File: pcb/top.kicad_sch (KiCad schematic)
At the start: 77 parts, among them J1 Conn_01x01, J10 Conn_01x01, J11 Conn_01x01, J2 Conn_01x01, J3 Conn_01x06, J4 Conn_01x01, J5 Conn_01x01, J6 Conn_01x01, J7 Conn_01x01, J8 Conn_01x01, J9 Conn_01x01, Q1 2N7002, Q2 2N7002, Q3 2N7002, Q4 2N7002, U1 L78L05_SOT89, U2 PIC12F629-ISN, U3 L78L08_SO8

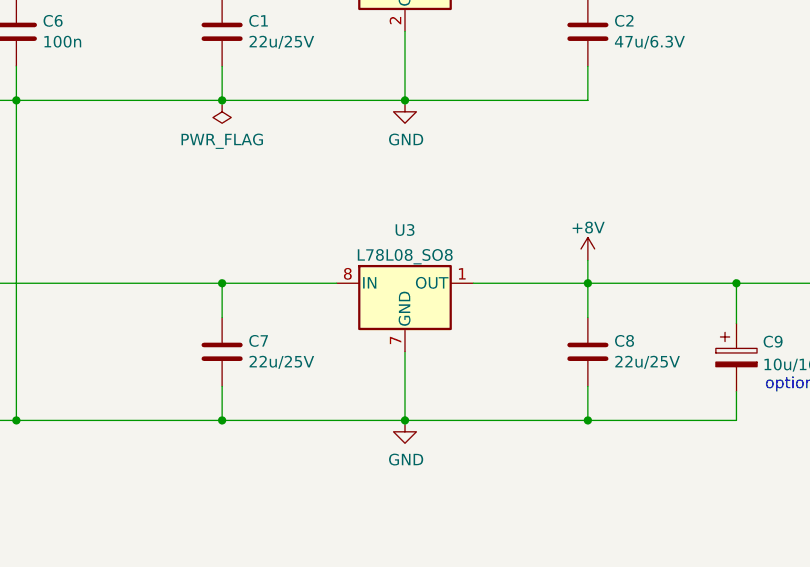
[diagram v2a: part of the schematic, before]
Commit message: Use SOT89 for 78L08.
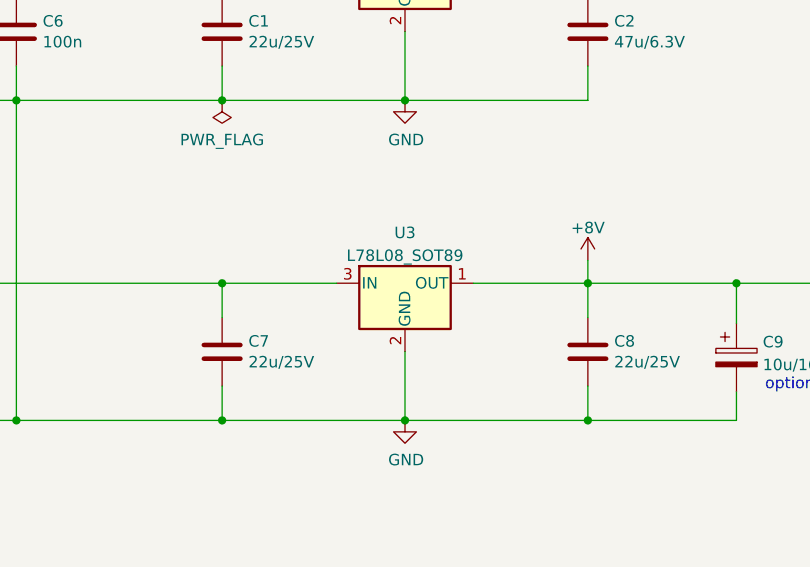
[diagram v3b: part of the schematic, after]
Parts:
- removed U3: L78L08_SO8, Package_SO:SOIC-8_3.9x4.9mm_P1.27mm, symbol Regulator_Linear:L78L08_SO8
- added U3: L78L08_SOT89, Package_TO_SOT_SMD:SOT-89-3_Handsoldering, symbol Regulator_Linear:L78L08_SOT89
- R1, R21: JLCPCB_IGNORE true -> (none); LCSC (none) -> C364154
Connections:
- net +15V: now also U3.3 (IN)
- net +8V: now also U3.1 (OUT)
- net GND: now also U3.2 (GND)
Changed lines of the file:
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@@
       (effects (font (size 1.27 1.27)) hide)
     )
-    (property "LCSC" "" (id 4) (at 67.31 81.28 0)
-      (effects (font (size 1.27 1.27)) hide)
-    )
-    (property "JLCPCB_IGNORE" "true" (id 5) (at 67.31 81.28 0)
+    (property "LCSC" "C364154" (id 4) (at 67.31 81.28 0)
+      (effects (font (size 1.27 1.27)) hide)
+    )
+    (property "JLCPCB_IGNORE" "" (id 5) (at 67.31 81.28 0)
       (effects (font (size 1.27 1.27)) hide)
     )
@@
     )
   )
-  (symbol (lib_id "Regulator_Linear:L78L08_SO8") (at 135.89 72.39 0) (unit 1)
+  (symbol (lib_id "Mechanical:MountingHole") (at 76.2 176.53 0) (unit 1)
+    (in_bom yes) (on_board yes)
+    (property "Reference" "H9" (id 0) (at 78.74 175.3616 0)
+      (effects (font (size 1.27 1.27)) (justify left))
+    )
+    (property "Value" "MountingHole" (id 1) (at 78.74 177.673 0)
+      (effects (font (size 1.27 1.27)) (justify left))
+    )
+    (property "Footprint" "MountingHole:MountingHole_2.2mm_M2" (id 2) (at 76.2 176.53 0)
+      (effects (font (size 1.27 1.27)) hide)
+    )
+    (property "Datasheet" "~" (id 3) (at 76.2 176.53 0)
+      (effects (font (size 1.27 1.27)) hide)
+    )
+    (property "JLCPCB_IGNORE" "true" (id 4) (at 76.2 176.53 0)
+      (effects (font (size 1.27 1.27)) hide)
+    )
+  )
+  (symbol (lib_id "Regulator_Linear:L78L08_SOT89") (at 135.89 72.39 0) (unit 1)
     (in_bom yes) (on_board yes) (fields_autoplaced)
-    (property "Reference" "U3" (id 0) (at 135.89 66.5185 0))
-    (property "Value" "L78L08_SO8" (id 1) (at 135.89 69.2936 0))
-    (property "Footprint" "Package_SO:SOIC-8_3.9x4.9mm_P1.27mm" (id 2) (at 138.43 67.31 0)
+    (property "Reference" "U3" (id 0) (at 135.89 66.7852 0))
+    (property "Value" "L78L08_SOT89" (id 1) (at 135.89 69.3221 0))
+    (property "Footprint" "Package_TO_SOT_SMD:SOT-89-3_Handsoldering" (id 2) (at 135.89 67.31 0)
       (effects (font (size 1.27 1.27) italic) hide)
     )
-    (property "Datasheet" "http://www.st.com/content/ccc/resource/technical/document/datasheet/15/55/e5/aa/23/5b/43/fd/CD00000446.pdf/files/CD00000446.pdf/jcr:content/translations/en.CD00000446.pdf" (id 3) (at 140.97 72.39 0)
+    (property "Datasheet" "http://www.st.com/content/ccc/resource/technical/document/datasheet/15/55/e5/aa/23/5b/43/fd/CD00000446.pdf/files/CD00000446.pdf/jcr:content/translations/en.CD00000446.pdf" (id 3) (at 135.89 73.66 0)
+      (effects (font (size 1.27 1.27)) hide)
+    )
+    (property "LCSC" "C122846" (id 4) (at 135.89 72.39 0)
       (effects (font (size 1.27 1.27)) hide)
     )
@@
     (pin "2")
     (pin "3")
-    (pin "4")
-    (pin "5")
-    (pin "6")
-    (pin "7")
-    (pin "8")
-  )
-  (symbol (lib_id "Mechanical:MountingHole") (at 76.2 176.53 0) (unit 1)
-    (in_bom yes) (on_board yes)
-    (property "Reference" "H9" (id 0) (at 78.74 175.3616 0)
-      (effects (font (size 1.27 1.27)) (justify left))
-    )
-    (property "Value" "MountingHole" (id 1) (at 78.74 177.673 0)
-      (effects (font (size 1.27 1.27)) (justify left))
-    )
-    (property "Footprint" "MountingHole:MountingHole_2.2mm_M2" (id 2) (at 76.2 176.53 0)
-      (effects (font (size 1.27 1.27)) hide)
-    )
-    (property "Datasheet" "~" (id 3) (at 76.2 176.53 0)
-      (effects (font (size 1.27 1.27)) hide)
-    )
-    (property "JLCPCB_IGNORE" "true" (id 4) (at 76.2 176.53 0)
-      (effects (font (size 1.27 1.27)) hide)
-    )
   )
   (symbol (lib_id "Device:R") (at 261.62 116.84 0) (mirror y) (unit 1)
@@
       (effects (font (size 1.27 1.27)) hide)
     )
-    (property "LCSC" "" (id 4) (at 261.62 116.84 0)
-      (effects (font (size 1.27 1.27)) hide)
-    )
-    (property "JLCPCB_IGNORE" "true" (id 5) (at 261.62 116.84 0)
+    (property "LCSC" "C364154" (id 4) (at 261.62 116.84 0)
+      (effects (font (size 1.27 1.27)) hide)
+    )
+    (property "JLCPCB_IGNORE" "" (id 5) (at 261.62 116.84 0)
       (effects (font (size 1.27 1.27)) hide)
     )
@@
       (reference "U2") (unit 1) (value "PIC12F629-ISN") (footprint "Package_SO:SOIC-8_3.9x4.9mm_P1.27mm")
     )
-    (path "/3b696e07-76f1-4f5e-aafe-cd6072c0e837"
-      (reference "U3") (unit 1) (value "L78L08_SO8") (footprint "Package_SO:SOIC-8_3.9x4.9mm_P1.27mm")
-    )
-  )
+    (path "/51343116-0c24-4c32-9cad-797ee49a352e"
+      (reference "U3") (unit 1) (value "L78L08_SOT89") (footprint "Package_TO_SOT_SMD:SOT-89-3_Handsoldering")
+    )
+  )

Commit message: Correct JLCPCB parts orientation.
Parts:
- U2: JLCPCB_CORRECTION (none) -> 0;0;-90
- U3: JLCPCB_CORRECTION (none) -> 0;0;180
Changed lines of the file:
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@@
+      (effects (font (size 1.27 1.27)) hide)
+    )
+    (property "JLCPCB_CORRECTION" "0;0;-90" (id 5) (at 152.4 135.89 0)
       (effects (font (size 1.27 1.27)) hide)
     )
@@
       (effects (font (size 1.27 1.27)) hide)
     )
+    (property "JLCPCB_CORRECTION" "0;0;180" (id 5) (at 135.89 72.39 0)
+      (effects (font (size 1.27 1.27)) hide)
+    )

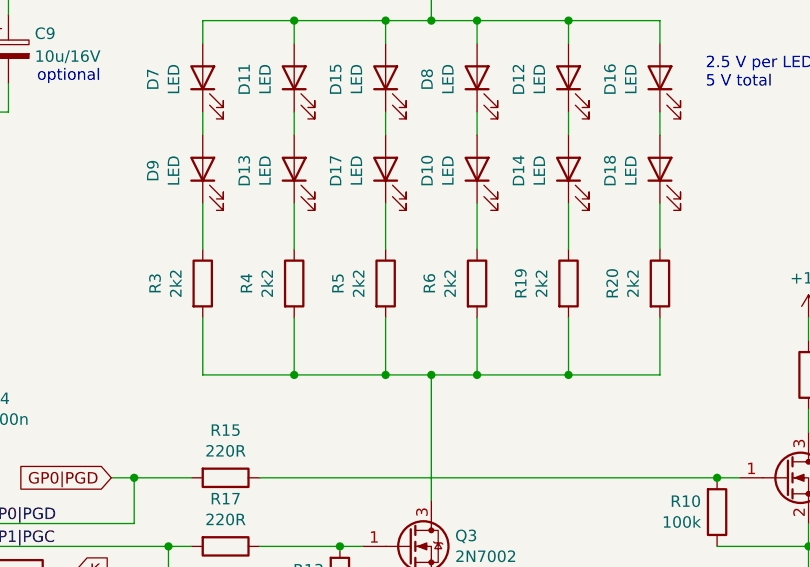
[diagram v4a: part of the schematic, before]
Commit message: Enalarge interior LEDs resistors to 4k7.
Light wa too bright.
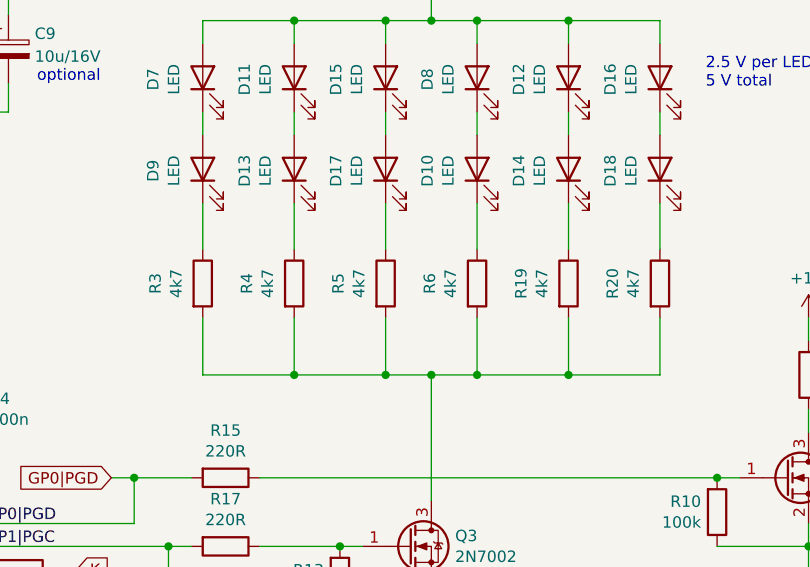
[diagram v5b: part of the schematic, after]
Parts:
- R19, R20, R3, R4, R5, R6: value 2k2 -> 4k7; LCSC C17520 -> C17673
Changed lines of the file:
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@@
     (in_bom yes) (on_board yes)
     (property "Reference" "R4" (id 0) (at 199.2122 106.68 90))
-    (property "Value" "2k2" (id 1) (at 201.5236 106.68 90))
+    (property "Value" "4k7" (id 1) (at 201.5236 106.68 90))
     (property "Footprint" "Resistor_SMD:R_0805_2012Metric_Pad1.20x1.40mm_HandSolder" (id 2) (at 202.692 106.68 90)
       (effects (font (size 1.27 1.27)) hide)
@@
       (effects (font (size 1.27 1.27)) hide)
     )
-    (property "LCSC" "C17520" (id 4) (at 204.47 106.68 0)
+    (property "LCSC" "C17673" (id 4) (at 204.47 106.68 0)
       (effects (font (size 1.27 1.27)) hide)
     )
@@
     (in_bom yes) (on_board yes)
     (property "Reference" "R3" (id 0) (at 189.0522 106.68 90))
-    (property "Value" "2k2" (id 1) (at 191.3636 106.68 90))
+    (property "Value" "4k7" (id 1) (at 191.3636 106.68 90))
     (property "Footprint" "Resistor_SMD:R_0805_2012Metric_Pad1.20x1.40mm_HandSolder" (id 2) (at 192.532 106.68 90)
       (effects (font (size 1.27 1.27)) hide)
@@
       (effects (font (size 1.27 1.27)) hide)
     )
-    (property "LCSC" "C17520" (id 4) (at 194.31 106.68 0)
+    (property "LCSC" "C17673" (id 4) (at 194.31 106.68 0)
       (effects (font (size 1.27 1.27)) hide)
     )
@@
     (in_bom yes) (on_board yes)
     (property "Reference" "R19" (id 0) (at 229.6922 106.68 90))
-    (property "Value" "2k2" (id 1) (at 232.0036 106.68 90))
+    (property "Value" "4k7" (id 1) (at 232.0036 106.68 90))
     (property "Footprint" "Resistor_SMD:R_0805_2012Metric_Pad1.20x1.40mm_HandSolder" (id 2) (at 233.172 106.68 90)
       (effects (font (size 1.27 1.27)) hide)
@@
       (effects (font (size 1.27 1.27)) hide)
     )
-    (property "LCSC" "C17520" (id 4) (at 234.95 106.68 0)
+    (property "LCSC" "C17673" (id 4) (at 234.95 106.68 0)
       (effects (font (size 1.27 1.27)) hide)
     )
@@
     (in_bom yes) (on_board yes)
     (property "Reference" "R5" (id 0) (at 209.3722 106.68 90))
-    (property "Value" "2k2" (id 1) (at 211.6836 106.68 90))
+    (property "Value" "4k7" (id 1) (at 211.6836 106.68 90))
     (property "Footprint" "Resistor_SMD:R_0805_2012Metric_Pad1.20x1.40mm_HandSolder" (id 2) (at 212.852 106.68 90)
       (effects (font (size 1.27 1.27)) hide)
@@
       (effects (font (size 1.27 1.27)) hide)
     )
-    (property "LCSC" "C17520" (id 4) (at 214.63 106.68 0)
+    (property "LCSC" "C17673" (id 4) (at 214.63 106.68 0)
       (effects (font (size 1.27 1.27)) hide)
     )
@@
     (in_bom yes) (on_board yes)
     (property "Reference" "R20" (id 0) (at 239.8522 106.68 90))
-    (property "Value" "2k2" (id 1) (at 242.1636 106.68 90))
+    (property "Value" "4k7" (id 1) (at 242.1636 106.68 90))
     (property "Footprint" "Resistor_SMD:R_0805_2012Metric_Pad1.20x1.40mm_HandSolder" (id 2) (at 243.332 106.68 90)
       (effects (font (size 1.27 1.27)) hide)
@@
       (effects (font (size 1.27 1.27)) hide)
     )
-    (property "LCSC" "C17520" (id 4) (at 245.11 106.68 0)
+    (property "LCSC" "C17673" (id 4) (at 245.11 106.68 0)
       (effects (font (size 1.27 1.27)) hide)
     )
@@
     (in_bom yes) (on_board yes)
     (property "Reference" "R6" (id 0) (at 219.5322 106.68 90))
-    (property "Value" "2k2" (id 1) (at 221.8436 106.68 90))
+    (property "Value" "4k7" (id 1) (at 221.8436 106.68 90))
     (property "Footprint" "Resistor_SMD:R_0805_2012Metric_Pad1.20x1.40mm_HandSolder" (id 2) (at 223.012 106.68 90)
       (effects (font (size 1.27 1.27)) hide)
@@
       (effects (font (size 1.27 1.27)) hide)
     )
-    (property "LCSC" "C17520" (id 4) (at 224.79 106.68 0)
+    (property "LCSC" "C17673" (id 4) (at 224.79 106.68 0)
       (effects (font (size 1.27 1.27)) hide)
     )
@@
     )
     (path "/00000000-0000-0000-0000-000061c84938"
-      (reference "R3") (unit 1) (value "2k2") (footprint "Resistor_SMD:R_0805_2012Metric_Pad1.20x1.40mm_HandSolder")
+      (reference "R3") (unit 1) (value "4k7") (footprint "Resistor_SMD:R_0805_2012Metric_Pad1.20x1.40mm_HandSolder")
     )
     (path "/00000000-0000-0000-0000-000061c84465"
-      (reference "R4") (unit 1) (value "2k2") (footprint "Resistor_SMD:R_0805_2012Metric_Pad1.20x1.40mm_HandSolder")
+      (reference "R4") (unit 1) (value "4k7") (footprint "Resistor_SMD:R_0805_2012Metric_Pad1.20x1.40mm_HandSolder")
     )
     (path "/d64eb0f9-9953-4bde-8f1f-742c06689809"
-      (reference "R5") (unit 1) (value "2k2") (footprint "Resistor_SMD:R_0805_2012Metric_Pad1.20x1.40mm_HandSolder")
+      (reference "R5") (unit 1) (value "4k7") (footprint "Resistor_SMD:R_0805_2012Metric_Pad1.20x1.40mm_HandSolder")
     )
     (path "/ffc018af-ade4-4519-807d-0355222f221a"
-      (reference "R6") (unit 1) (value "2k2") (footprint "Resistor_SMD:R_0805_2012Metric_Pad1.20x1.40mm_HandSolder")
+      (reference "R6") (unit 1) (value "4k7") (footprint "Resistor_SMD:R_0805_2012Metric_Pad1.20x1.40mm_HandSolder")
     )
     (path "/00000000-0000-0000-0000-000061cacce2"
@@
     )
     (path "/9aa007b8-f176-4a83-baec-308581049200"
-      (reference "R19") (unit 1) (value "2k2") (footprint "Resistor_SMD:R_0805_2012Metric_Pad1.20x1.40mm_HandSolder")
+      (reference "R19") (unit 1) (value "4k7") (footprint "Resistor_SMD:R_0805_2012Metric_Pad1.20x1.40mm_HandSolder")
     )
     (path "/dc625149-4b9e-4e62-9f3c-a8ad9ac6b0e2"
-      (reference "R20") (unit 1) (value "2k2") (footprint "Resistor_SMD:R_0805_2012Metric_Pad1.20x1.40mm_HandSolder")
+      (reference "R20") (unit 1) (value "4k7") (footprint "Resistor_SMD:R_0805_2012Metric_Pad1.20x1.40mm_HandSolder")
     )
     (path "/5ed39f78-a424-4fab-b48b-d1e85e43d60d"

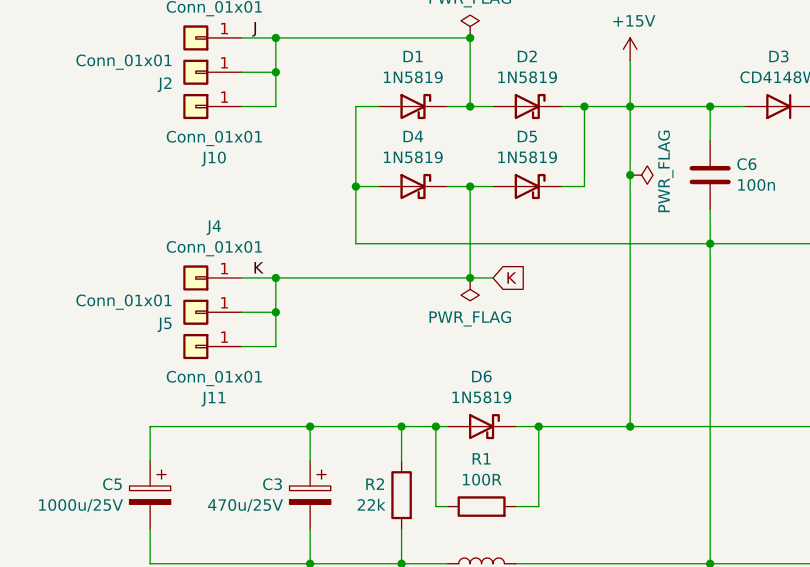
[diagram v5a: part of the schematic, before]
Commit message: Add fuse on input.
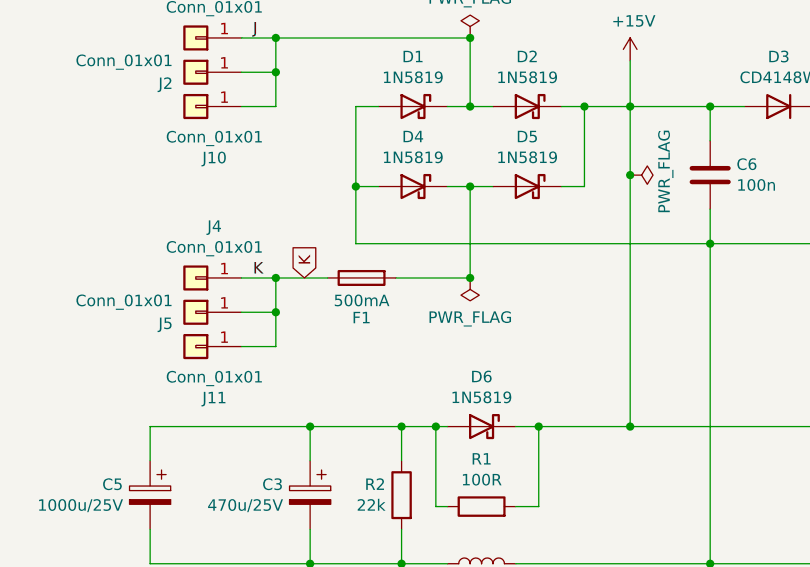
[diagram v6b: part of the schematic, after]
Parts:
- added F1: 500mA, Fuse:Fuse_1206_3216Metric_Pad1.42x1.75mm_HandSolder, symbol Device:Fuse
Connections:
- net K: now also F1.1; no longer D4.1 (K), D5.2 (A)
- new net: D4.1 (K), D5.2 (A), F1.2
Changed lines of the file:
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@@
-    (stroke (width 0) (type default) (color 0 0 0 0))
-  )
-  (wire (pts (xy 66.04 55.88) (xy 68.58 55.88))
     (stroke (width 0) (type default) (color 0 0 0 0))
   )
@@
     (stroke (width 0) (type default) (color 0 0 0 0))
   )
-  (wire (pts (xy 44.45 55.88) (xy 66.04 55.88))
+  (wire (pts (xy 44.45 55.88) (xy 50.165 55.88))
     (stroke (width 0) (type default) (color 0 0 0 0))
   )
@@
   )
   (wire (pts (xy 152.4 116.84) (xy 167.64 116.84))
+    (stroke (width 0) (type default) (color 0 0 0 0))
+  )
+  (wire (pts (xy 57.785 55.88) (xy 66.04 55.88))
     (stroke (width 0) (type default) (color 0 0 0 0))
   )
@@
     )
   )
-  (global_label "K" (shape input) (at 68.58 55.88 0) (fields_autoplaced)
+  (global_label "K" (shape input) (at 47.625 55.88 90) (fields_autoplaced)
     (effects (font (size 1.27 1.27)) (justify left))
-    (property "Intersheet References" "${INTERSHEET_REFS}" (id 0) (at 2.54 0 0)
+    (property "Intersheet References" "${INTERSHEET_REFS}" (id 0) (at -8.255 121.92 0)
       (effects (font (size 1.27 1.27)) hide)
     )
@@
     (pin "1")
   )
+  (symbol (lib_id "Device:Fuse") (at 53.975 55.88 90) (mirror x) (unit 1)
+    (in_bom yes) (on_board yes)
+    (property "Reference" "F1" (id 0) (at 53.975 60.325 90))
+    (property "Value" "500mA" (id 1) (at 53.975 58.42 90))
+    (property "Footprint" "Fuse:Fuse_1206_3216Metric_Pad1.42x1.75mm_HandSolder" (id 2) (at 53.975 54.102 90)
+      (effects (font (size 1.27 1.27)) hide)
+    )
+    (property "Datasheet" "~" (id 3) (at 53.975 55.88 0)
+      (effects (font (size 1.27 1.27)) hide)
+    )
+    (property "LCSC" "C136341" (id 4) (at 53.975 55.88 0)
+      (effects (font (size 1.27 1.27)) hide)
+    )
+    (pin "1")
+    (pin "2")
+  )
   (symbol (lib_id "power:+8V") (at 69.85 111.76 0) (unit 1)
     (in_bom yes) (on_board yes) (fields_autoplaced)
@@
       (reference "D18") (unit 1) (value "LED") (footprint "LED_SMD:LED_PLCC_2835_Handsoldering")
     )
+    (path "/6386684e-c2b7-4e4c-9bf1-a4f9d3d37a0d"
+      (reference "F1") (unit 1) (value "500mA") (footprint "Fuse:Fuse_1206_3216Metric_Pad1.42x1.75mm_HandSolder")
+    )
     (path "/00000000-0000-0000-0000-000061ca32f4"
